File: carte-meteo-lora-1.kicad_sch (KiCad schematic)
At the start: 80 parts, among them J1 Conn_01x04, J2 USB_C_Receptacle_USB2.0_14P, J4 Conn_01x04_Pin, Q1 Q_NMOS, Q2 Q_NMOS, SW1 SW_SPST, U14 TMP117AIDRV, U2 BQ77905, U3 HS96L03W2C03, U4 ESP32-S3FN8, U5 LDL212PV33R, Y1 48M

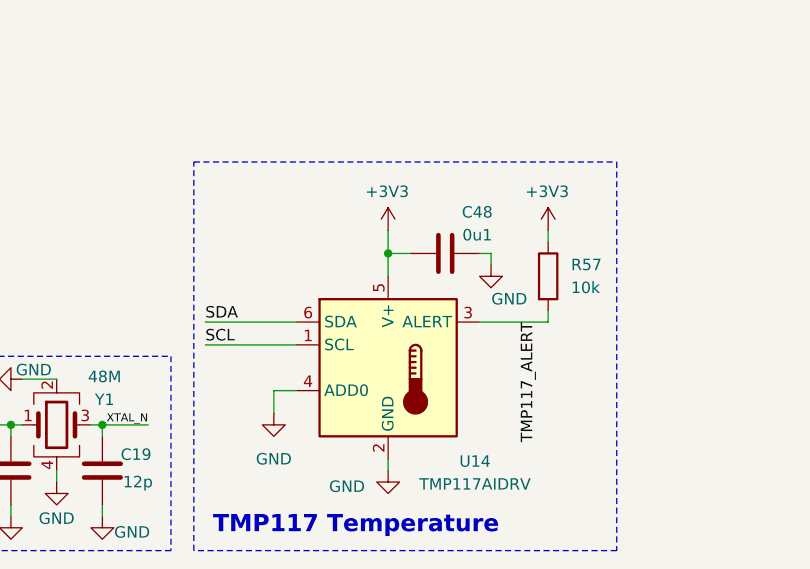
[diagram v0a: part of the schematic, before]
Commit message: remove TMP117 temp sensor
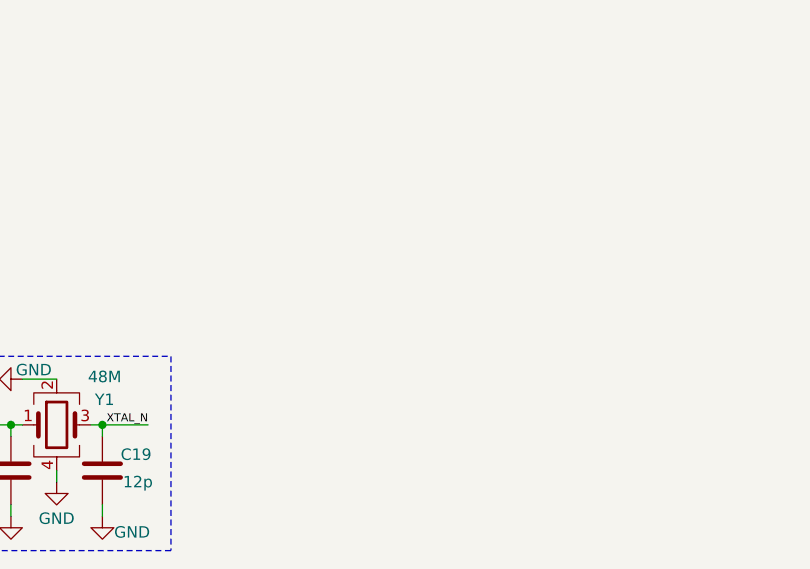
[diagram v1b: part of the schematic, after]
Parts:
- removed C48: 0u1, Capacitor_SMD:C_0402_1005Metric, symbol Device:C
- removed R57: 10k, Resistor_SMD:R_0402_1005Metric, symbol Device:R
- removed U14: TMP117AIDRV, Package_SON:WSON-6-1EP_2x2mm_P0.65mm_EP1x1.6mm, symbol Sensor_Temperature:TMP117xxDRV
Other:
- note removed: "TMP117 Temperature"

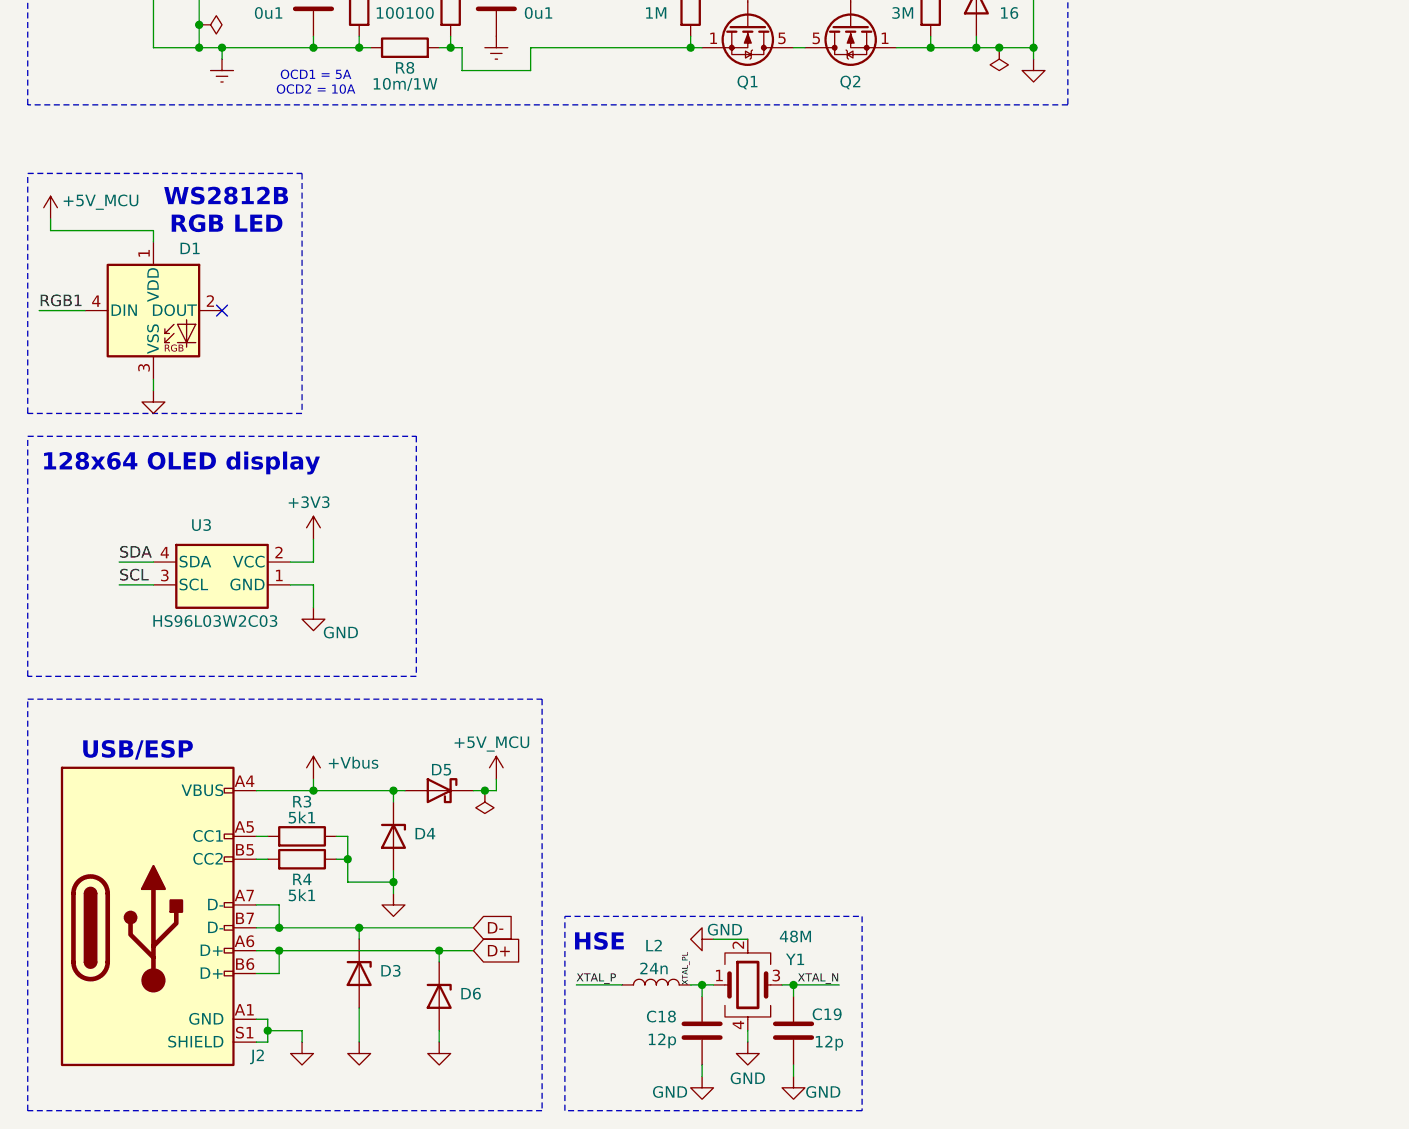
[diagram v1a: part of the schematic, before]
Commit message: schem: add MS5607 Pressure sensor
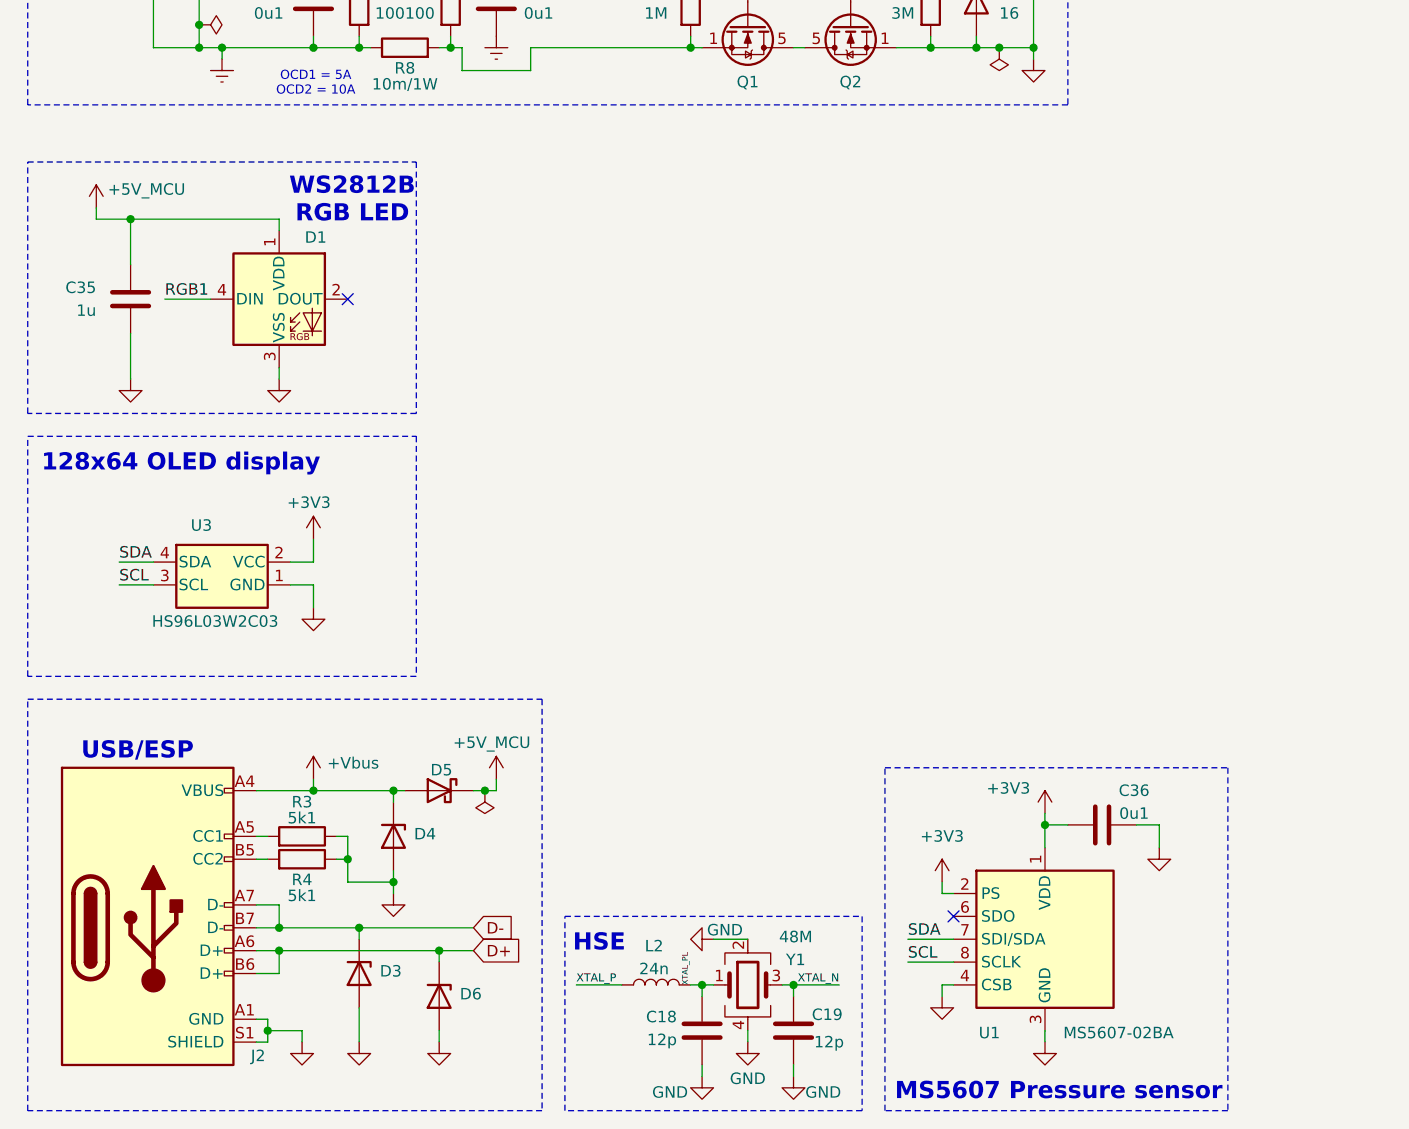
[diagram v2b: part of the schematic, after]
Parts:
- added C35: 1u, Capacitor_SMD:C_0402_1005Metric, symbol Device:C
- added C36: 0u1, Capacitor_SMD:C_0402_1005Metric, symbol Device:C
- added U1: MS5607-02BA, Package_LGA:LGA-8_3x5mm_P1.25mm, symbol Sensor_Pressure:MS5607-02BA
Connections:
- net +3V3: now also C36.2, U1.1 (VDD), U1.2 (PS)
- net +5V_MCU: now also C35.1
- net GND: now also C35.2, C36.1, U1.3 (GND), U1.4 (CSB), U1.5 (CSB)
- net SCL: now also U1.8 (SCLK)
- net SDA: now also U1.7 (SDI/SDA)
- no-connect marks 22 -> 23
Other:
- note added: "MS5607 Pressure sensor"
- moved on the sheet: D1

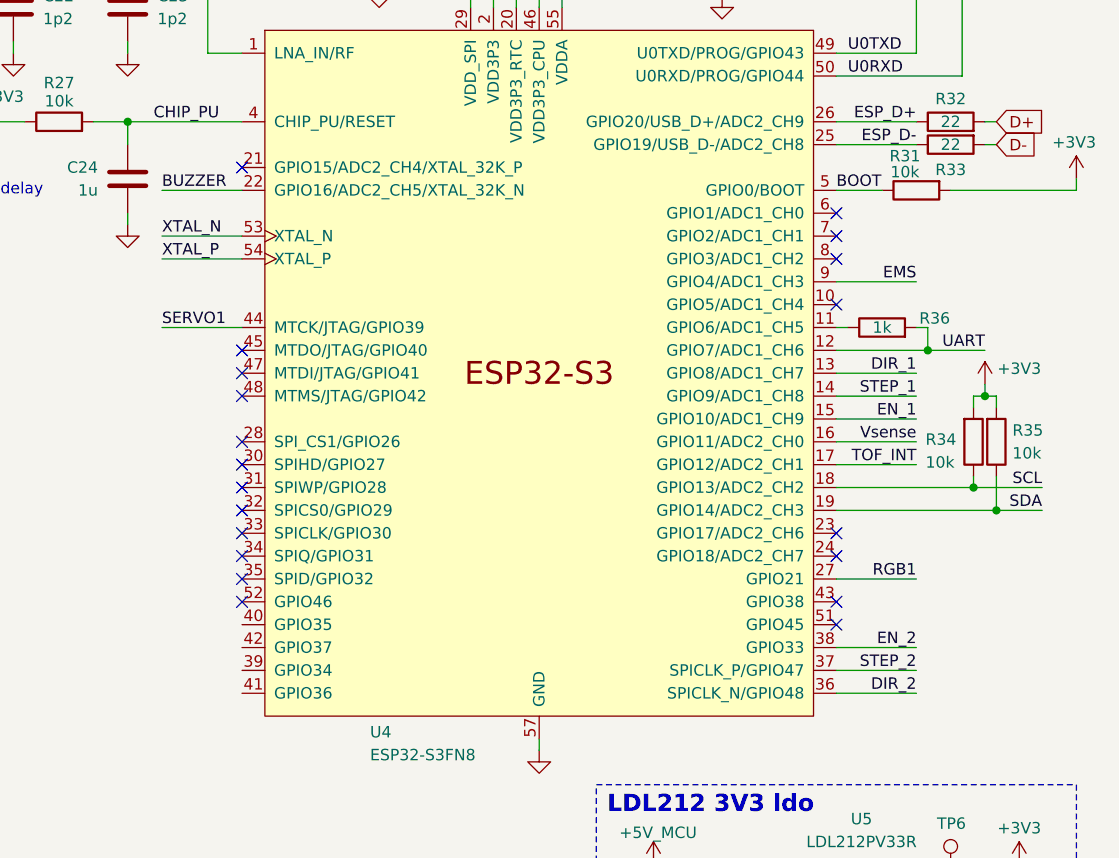
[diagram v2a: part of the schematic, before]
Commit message: schem: remove old gpios
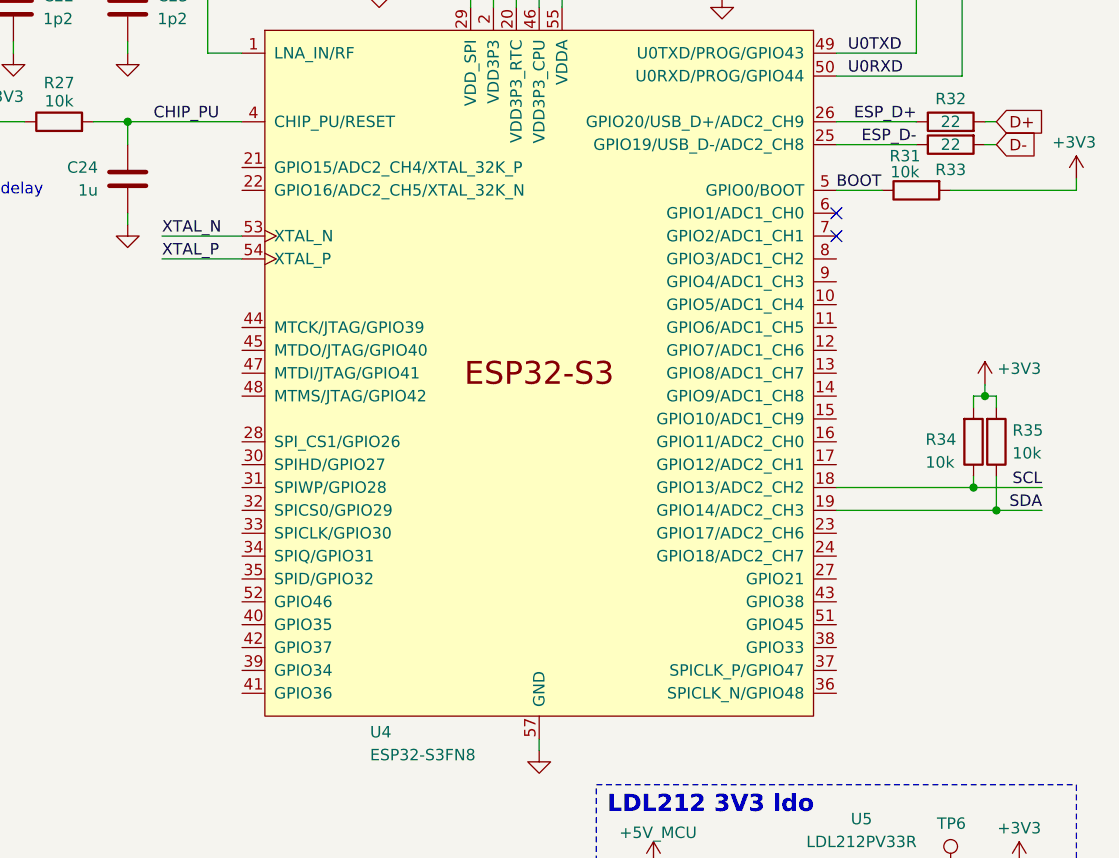
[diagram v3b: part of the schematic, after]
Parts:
- removed R36: 1k, Resistor_SMD:R_0402_1005Metric, symbol Device:R
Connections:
- net RGB1: no longer U4.27 (GPIO21)
- net BUZZER: no longer names the net of U4.22 (GPIO16/ADC2_CH5/XTAL_32K_N)
- net DIR_1: no longer names the net of U4.13 (GPIO8/ADC1_CH7)
- net DIR_2: no longer names the net of U4.36 (SPICLK_N/GPIO48)
- net EMS: no longer names the net of U4.9 (GPIO4/ADC1_CH3)
- net EN_1: no longer names the net of U4.15 (GPIO10/ADC1_CH9)
- net EN_2: no longer names the net of U4.38 (GPIO33)
- net SERVO1: no longer names the net of U4.44 (MTCK/JTAG/GPIO39)
- net STEP_1: no longer names the net of U4.14 (GPIO9/ADC1_CH8)
- net STEP_2: no longer names the net of U4.37 (SPICLK_P/GPIO47)
- net TOF_INT: no longer names the net of U4.17 (GPIO12/ADC2_CH1)
- net UART: no longer names the net of U4.12 (GPIO7/ADC1_CH6)
- net Vsense: no longer names the net of U4.16 (GPIO11/ADC2_CH0)
- no-connect marks 23 -> 5

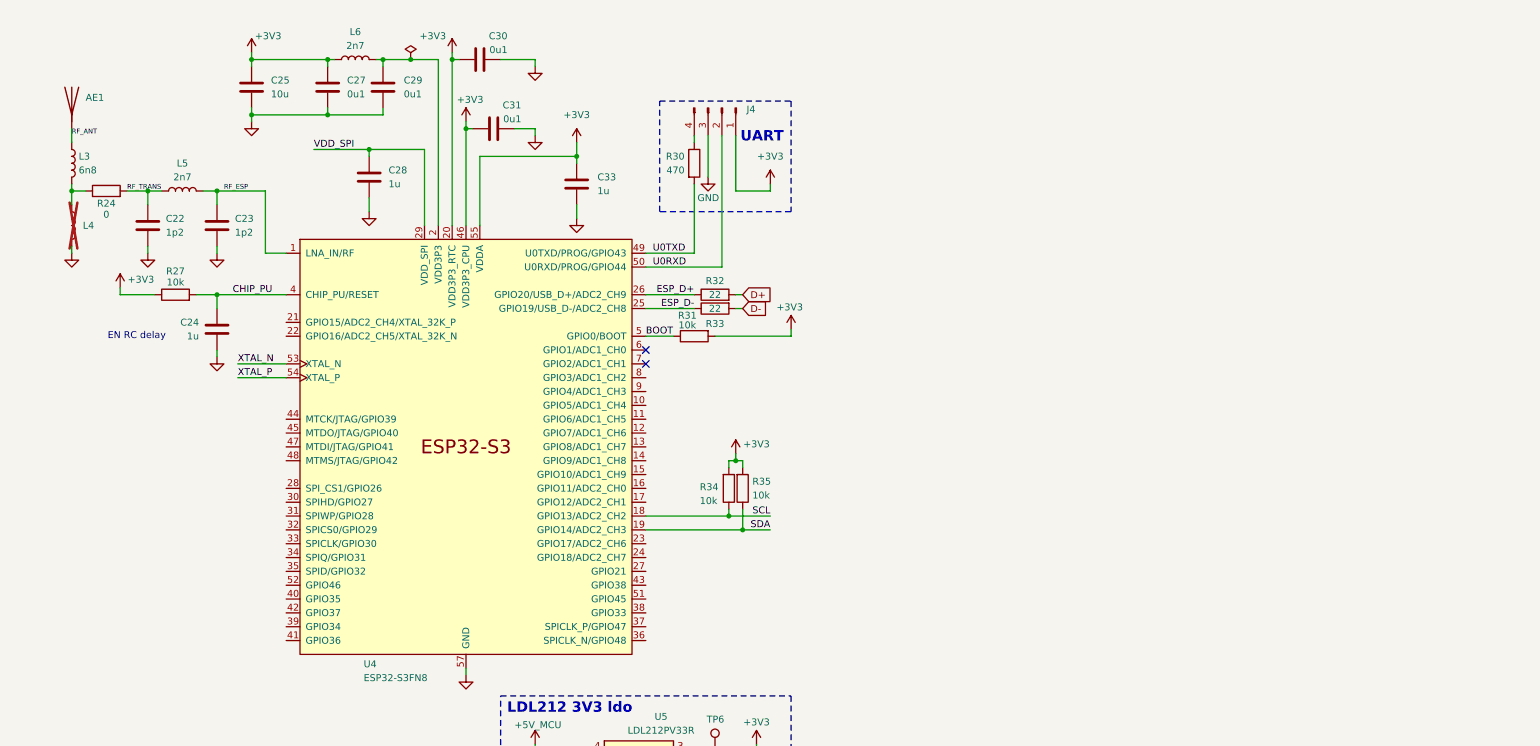
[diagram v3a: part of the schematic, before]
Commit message: schem: add esp32-c5 with decoupling caps
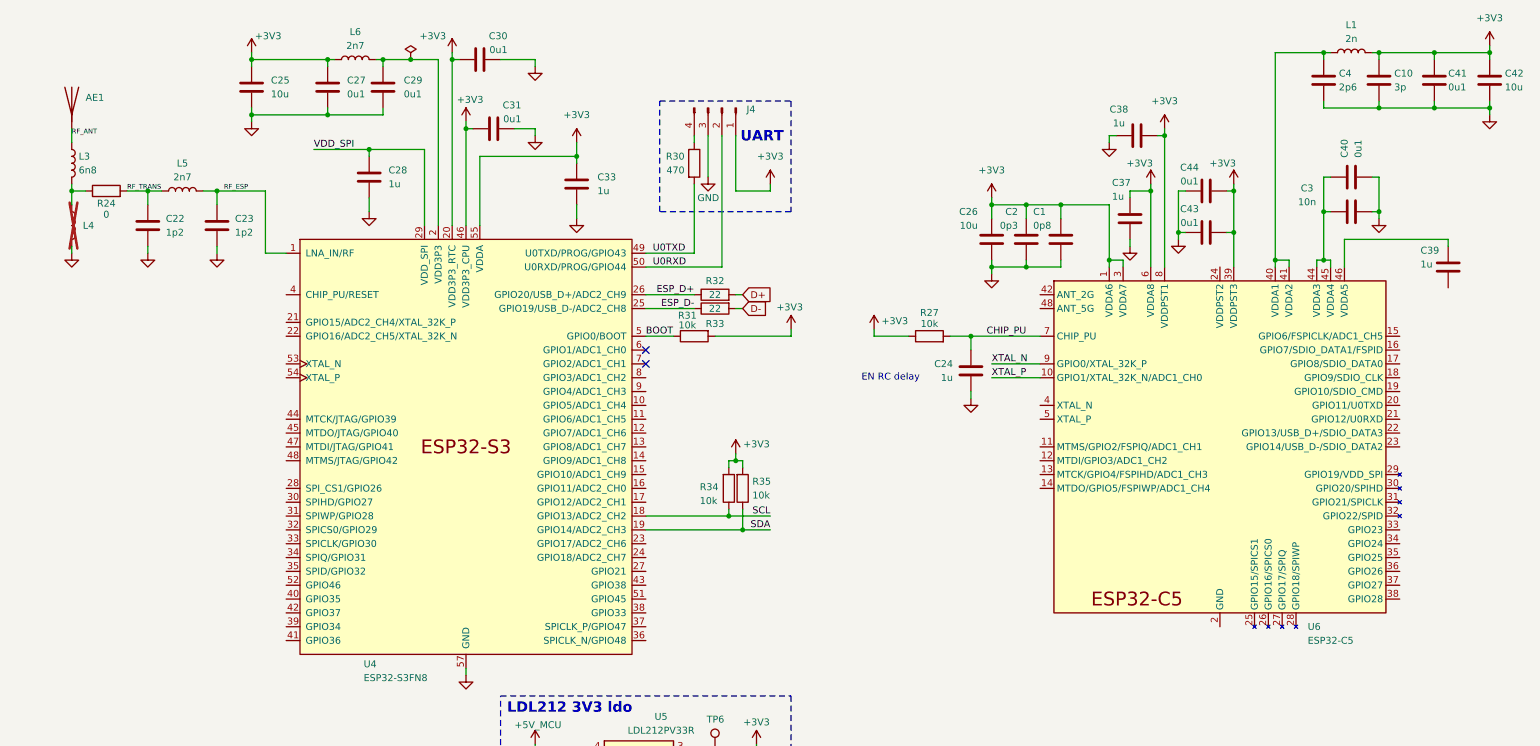
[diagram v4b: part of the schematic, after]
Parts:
- added C1: 0p8, symbol Device:C
- added C10: 3p, symbol Device:C
- added C2: 0p3, symbol Device:C
- added C26, C42: 10u, Capacitor_SMD:C_0402_1005Metric, symbol Device:C
- added C3: 10n, symbol Device:C
- added C37, C38, C39: 1u, Capacitor_SMD:C_0402_1005Metric, symbol Device:C
- added C4: 2p6, symbol Device:C
- added C40, C41, C43, C44: 0u1, Capacitor_SMD:C_0402_1005Metric, symbol Device:C
- added L1: 2n, symbol Device:L
- added U6: ESP32-C5, Package_DFN_QFN:QFN-48-1EP_6x6mm_P0.4mm_EP4.6x4.6mm, symbol GLCS:ESP32-C5
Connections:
- net +3V3: now also C1.1, C10.1, C2.1, C26.1, C37.2, C38.2, C41.1, C42.1, C43.2, C44.2, L1.2, U6.1 (VDDA6), U6.3 (VDDA7), U6.39 (VDDPST3), U6.6 (VDDA8), U6.8 (VDDPST1)
- net CHIP_PU: now also U6.7 (CHIP_PU); no longer U4.4 (CHIP_PU/RESET)
- net GND: now also C1.2, C10.2, C2.2, C26.2, C3.2, C37.1, C38.1, C4.2, C40.2, C41.2, C42.2, C43.1, C44.1, U6.2 (GND), U6.43 (GND), U6.47 (GND), U6.49 (GND)
- net XTAL_N: now also U6.9 (GPIO0/XTAL_32K_P); no longer U4.53 (XTAL_N)
- net XTAL_P: now also U6.10 (GPIO1/XTAL_32K_N/ADC1_CH0); no longer U4.54 (XTAL_P)
- new net: C4.1, L1.1, U6.40 (VDDA1), U6.41 (VDDA2)
- new net: C3.1, C40.1, U6.44 (VDDA3), U6.45 (VDDA4)
- new net: C39.2, U6.46 (VDDA5)
